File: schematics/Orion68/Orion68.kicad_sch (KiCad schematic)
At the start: 0 parts

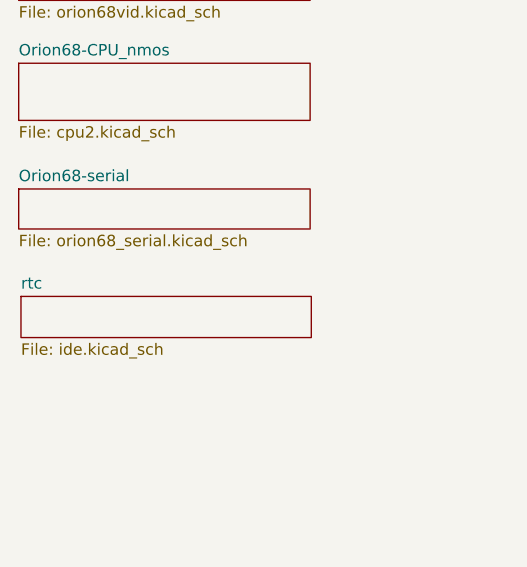
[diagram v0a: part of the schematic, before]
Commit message: Changed dtack system
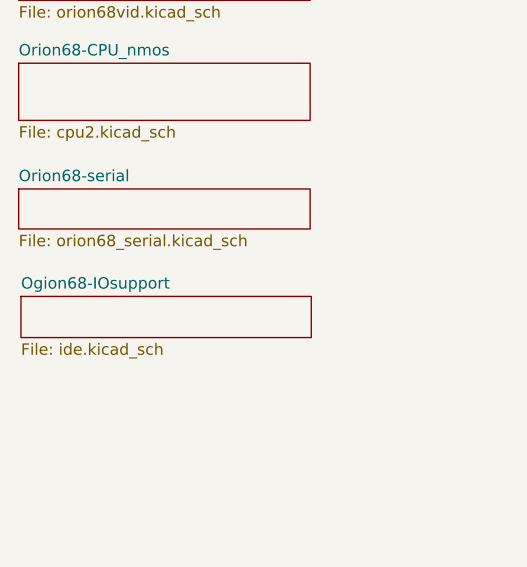
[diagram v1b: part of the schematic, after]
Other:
- sheet rtc renamed Ogion68-IOsupport
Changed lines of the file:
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@@
 			(color 0 0 0 0.0000)
 		)
-		(property "Sheetname" "rtc"
+		(property "Sheetname" "Ogion68-IOsupport"
 			(at 19.304 102.6664 0)
 			(effects

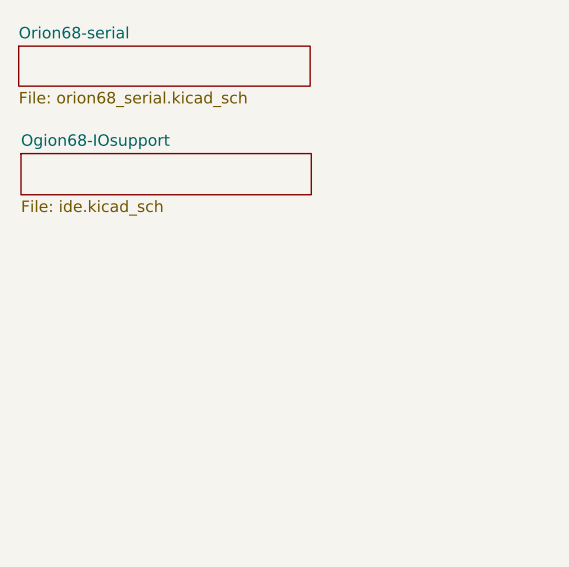
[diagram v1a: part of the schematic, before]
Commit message: Power control implemented
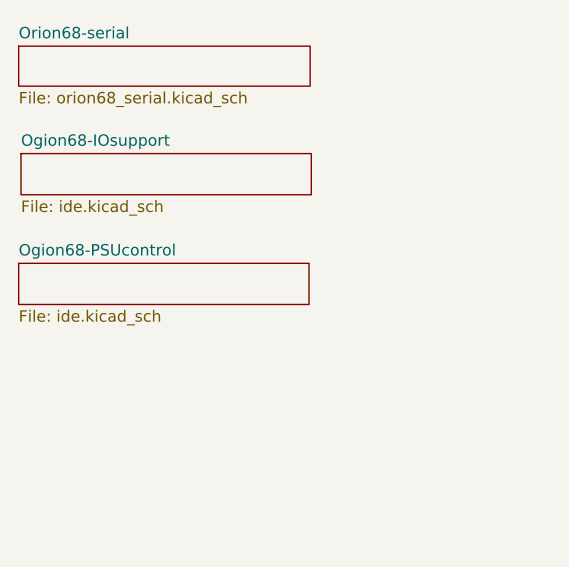
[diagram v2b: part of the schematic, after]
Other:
- added sheet Ogion68-PSUcontrol (ide.kicad_sch)
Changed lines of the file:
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@@
+	)
+	(sheet
+		(at 19.05 115.57)
+		(size 32.258 4.572)
+		(exclude_from_sim no)
+		(in_bom yes)
+		(on_board yes)
+		(dnp no)
+		(fields_autoplaced yes)
+		(stroke
+			(width 0.1524)
+			(type solid)
+		)
+		(fill
+			(color 0 0 0 0.0000)
+		)
+		(property "Sheetname" "Ogion68-PSUcontrol"
+			(at 19.05 114.8584 0)
+			(effects
+				(font
+					(size 1.27 1.27)
+				)
+				(justify left bottom)
+			)
+		)
+		(property "Sheetfile" "ide.kicad_sch"
+			(at 19.05 120.7266 0)
+			(effects
+				(font
+					(size 1.27 1.27)
+				)
+				(justify left top)
+			)
+		)
+		(instances
+			(project "Orion68"
+				(path "/c7ab032b-c937-44de-ab42-c91dee57f0a8"
+					(page "2")
+				)
+			)
+		)
 	)
 	(sheet
